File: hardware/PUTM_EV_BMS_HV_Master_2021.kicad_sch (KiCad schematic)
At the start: 22 parts, among them SW1 RESET, U19 STM32F446RETx, Y1 20MHz, Y2 32.768kHz

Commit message: 3d models update, more work on pcb
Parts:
- removed Y2: 32.768kHz, Crystal:Crystal_SMD_3225-4Pin_3.2x2.5mm, symbol Device:Crystal_GND24_Small
- added Y2: 32.768kHz, Crystal:Crystal_SMD_3215-2Pin_3.2x1.5mm, symbol Device:Crystal_Small
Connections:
- net RTC_CLK_IN: now also Y2.2
- net RTC_CLK_OUT: now also Y2.1
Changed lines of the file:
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@@
   (junction (at 252.73 152.4) (diameter 0) (color 0 0 0 0)
-  )
-  (junction (at 245.11 148.59) (diameter 0) (color 0 0 0 0)
   )
   (junction (at 60.96 35.56) (diameter 0) (color 0 0 0 0)
@@
     (stroke (width 0) (type default) (color 0 0 0 0))
   )
-  (wire (pts (xy 245.11 148.59) (xy 245.11 152.4))
-    (stroke (width 0) (type default) (color 0 0 0 0))
-  )
   (wire (pts (xy 117.475 187.325) (xy 118.745 187.325))
     (stroke (width 0) (type default) (color 0 0 0 0))
@@
     (stroke (width 0) (type default) (color 0 0 0 0))
   )
-  (wire (pts (xy 245.11 144.78) (xy 245.11 148.59))
+  (wire (pts (xy 245.11 144.78) (xy 245.11 152.4))
     (stroke (width 0) (type default) (color 0 0 0 0))
   )
@@
     (stroke (width 0) (type default) (color 0 0 0 0))
   )
-  (wire (pts (xy 255.27 148.59) (xy 256.54 148.59))
-    (stroke (width 0) (type default) (color 0 0 0 0))
-  )
   (wire (pts (xy 139.065 147.955) (xy 137.795 147.955))
     (stroke (width 0) (type default) (color 0 0 0 0))
@@
   )
   (wire (pts (xy 38.1 118.11) (xy 40.64 118.11))
-    (stroke (width 0) (type default) (color 0 0 0 0))
-  )
-  (wire (pts (xy 245.11 148.59) (xy 250.19 148.59))
     (stroke (width 0) (type default) (color 0 0 0 0))
   )
@@
     (pin "1")
   )
-  (symbol (lib_id "power:GND") (at 256.54 148.59 90) (unit 1)
-    (in_bom yes) (on_board yes)
-    (property "Reference" "#PWR0166" (id 0) (at 262.89 148.59 0)
-      (effects (font (size 1.27 1.27)) hide)
-    )
-    (property "Value" "GND" (id 1) (at 259.7912 148.463 90)
-      (effects (font (size 1.27 1.27)) (justify right))
-    )
-    (property "Footprint" "" (id 2) (at 256.54 148.59 0)
-      (effects (font (size 1.27 1.27)) hide)
-    )
-    (property "Datasheet" "" (id 3) (at 256.54 148.59 0)
-      (effects (font (size 1.27 1.27)) hide)
-    )
-    (pin "1")
-  )
   (symbol (lib_id "power:GND") (at 224.155 148.59 90) (unit 1)
     (in_bom yes) (on_board yes)
@@
     (pin "4")
   )
-  (symbol (lib_id "Device:Crystal_GND24_Small") (at 252.73 148.59 90) (unit 1)
-    (in_bom yes) (on_board yes)
-    (property "Reference" "Y2" (id 0) (at 255.27 139.7 90))
-    (property "Value" "32.768kHz" (id 1) (at 257.81 141.605 90))
-    (property "Footprint" "Crystal:Crystal_SMD_3225-4Pin_3.2x2.5mm" (id 2) (at 252.73 148.59 0)
+  (symbol (lib_id "Device:Crystal_Small") (at 252.73 148.59 90) (unit 1)
+    (in_bom yes) (on_board yes) (fields_autoplaced)
+    (property "Reference" "Y2" (id 0) (at 255.27 147.3199 90)
+      (effects (font (size 1.27 1.27)) (justify right))
+    )
+    (property "Value" "32.768kHz" (id 1) (at 255.27 149.8599 90)
+      (effects (font (size 1.27 1.27)) (justify right))
+    )
+    (property "Footprint" "Crystal:Crystal_SMD_3215-2Pin_3.2x1.5mm" (id 2) (at 252.73 148.59 0)
       (effects (font (size 1.27 1.27)) hide)
     )
@@
     (pin "1")
     (pin "2")
-    (pin "3")
-    (pin "4")
   )
   (sheet (at 239.395 40.64) (size 26.035 7.62) (fields_autoplaced)
@@
       (reference "#PWR0165") (unit 1) (value "+3.3V") (footprint "")
     )
-    (path "/3bcc80e3-9948-4ec4-868e-16f831c1e740"
-      (reference "#PWR0166") (unit 1) (value "GND") (footprint "")
-    )
     (path "/e61cc821-5479-4c04-b5ab-4a32f17b4f03/3f43c004-d17f-43ac-98bf-c5e9bce1100f"
       (reference "#PWR0167") (unit 1) (value "GND") (footprint "")
@@
       (reference "#PWR0173") (unit 1) (value "GND") (footprint "")
     )
+    (path "/568caa85-d8c4-4885-aabf-c5422dff8b33/5428d4f5-a135-4ff7-981d-717e6e459bc5"
+      (reference "#PWR0174") (unit 1) (value "ISO_GND") (footprint "")
+    )
+    (path "/568caa85-d8c4-4885-aabf-c5422dff8b33/bcd60228-1ed8-4c6e-a1e8-d1f398832a01"
+      (reference "#PWR0175") (unit 1) (value "ISO_GND") (footprint "")
+    )
+    (path "/568caa85-d8c4-4885-aabf-c5422dff8b33/0ac2b524-275c-4685-9499-8b49e50152b4"
+      (reference "#PWR0176") (unit 1) (value "ISO_GND") (footprint "")
+    )
     (path "/6eb4a2b1-8e5b-451b-b593-8aaaa3a4213e/7b3cb172-90a4-4003-9a24-8fe28b6c8d7e"
       (reference "#PWR0184") (unit 1) (value "+5V") (footprint "")
@@
       (reference "#PWR0190") (unit 1) (value "ISO_GND") (footprint "")
     )
-    (path "/568caa85-d8c4-4885-aabf-c5422dff8b33/0ac2b524-275c-4685-9499-8b49e50152b4"
-      (reference "#PWR?") (unit 1) (value "ISO_GND") (footprint "")
-    )
-    (path "/568caa85-d8c4-4885-aabf-c5422dff8b33/5428d4f5-a135-4ff7-981d-717e6e459bc5"
-      (reference "#PWR?") (unit 1) (value "ISO_GND") (footprint "")
-    )
-    (path "/568caa85-d8c4-4885-aabf-c5422dff8b33/bcd60228-1ed8-4c6e-a1e8-d1f398832a01"
-      (reference "#PWR?") (unit 1) (value "ISO_GND") (footprint "")
-    )
     (path "/66c3869d-de11-4d8d-b4de-9d98c32ec205/ddeb9dfe-eb2d-4bf5-bf14-a97849901813"
       (reference "BT1") (unit 1) (value "KEYSTONE 103") (footprint "Battery:BatteryHolder_Keystone_103_1x20mm")
@@
       (reference "L3") (unit 1) (value "33uH") (footprint "Inductor_SMD:L_12x12mm_H8mm")
     )
-    (path "/66c3869d-de11-4d8d-b4de-9d98c32ec205/97f31275-08a9-4ef1-ab6a-111397d3a2f7"
-      (reference "L4") (unit 1) (value "NLV32T-220J-PF") (footprint "Inductor_SMD:L_1210_3225Metric")
-    )
-    (path "/e61cc821-5479-4c04-b5ab-4a32f17b4f03/87282ca0-3147-4352-a9e5-29f84b0fe51e"
-      (reference "L5") (unit 1) (value "NLV32T-220J-PF") (footprint "Inductor_SMD:L_1210_3225Metric")
+    (path "/66c3869d-de11-4d8d-b4de-9d98c32ec205/eb503f36-06f9-429b-bfac-69b2fc2fa2db"
+      (reference "L4") (unit 1) (value "6.8uH") (footprint "Inductor_SMD:L_1206_3216Metric")
+    )
+    (path "/e61cc821-5479-4c04-b5ab-4a32f17b4f03/0422bc5c-79a8-49f4-a2a4-8342195de570"
+      (reference "L5") (unit 1) (value "6.8uH") (footprint "Inductor_SMD:L_1206_3216Metric")
     )
     (path "/81dc0685-0bdd-4dc2-8f76-92836044cf1e/b8954743-0175-4ee0-bad0-8f0716e13306/591c3187-ead2-446d-b183-7d5f2d76f3df"
@@
       (reference "Y1") (unit 1) (value "20MHz") (footprint "Crystal:Crystal_SMD_3225-4Pin_3.2x2.5mm")
     )
-    (path "/b803fbf4-9ceb-446d-ade7-ea57730cfc5e"
-      (reference "Y2") (unit 1) (value "32.768kHz") (footprint "Crystal:Crystal_SMD_3225-4Pin_3.2x2.5mm")
-    )
-  )
+    (path "/ee6556f0-1d2b-4352-82ce-d8d308cb643b"
+      (reference "Y2") (unit 1) (value "32.768kHz") (footprint "Crystal:Crystal_SMD_3215-2Pin_3.2x1.5mm")
+    )
+  )

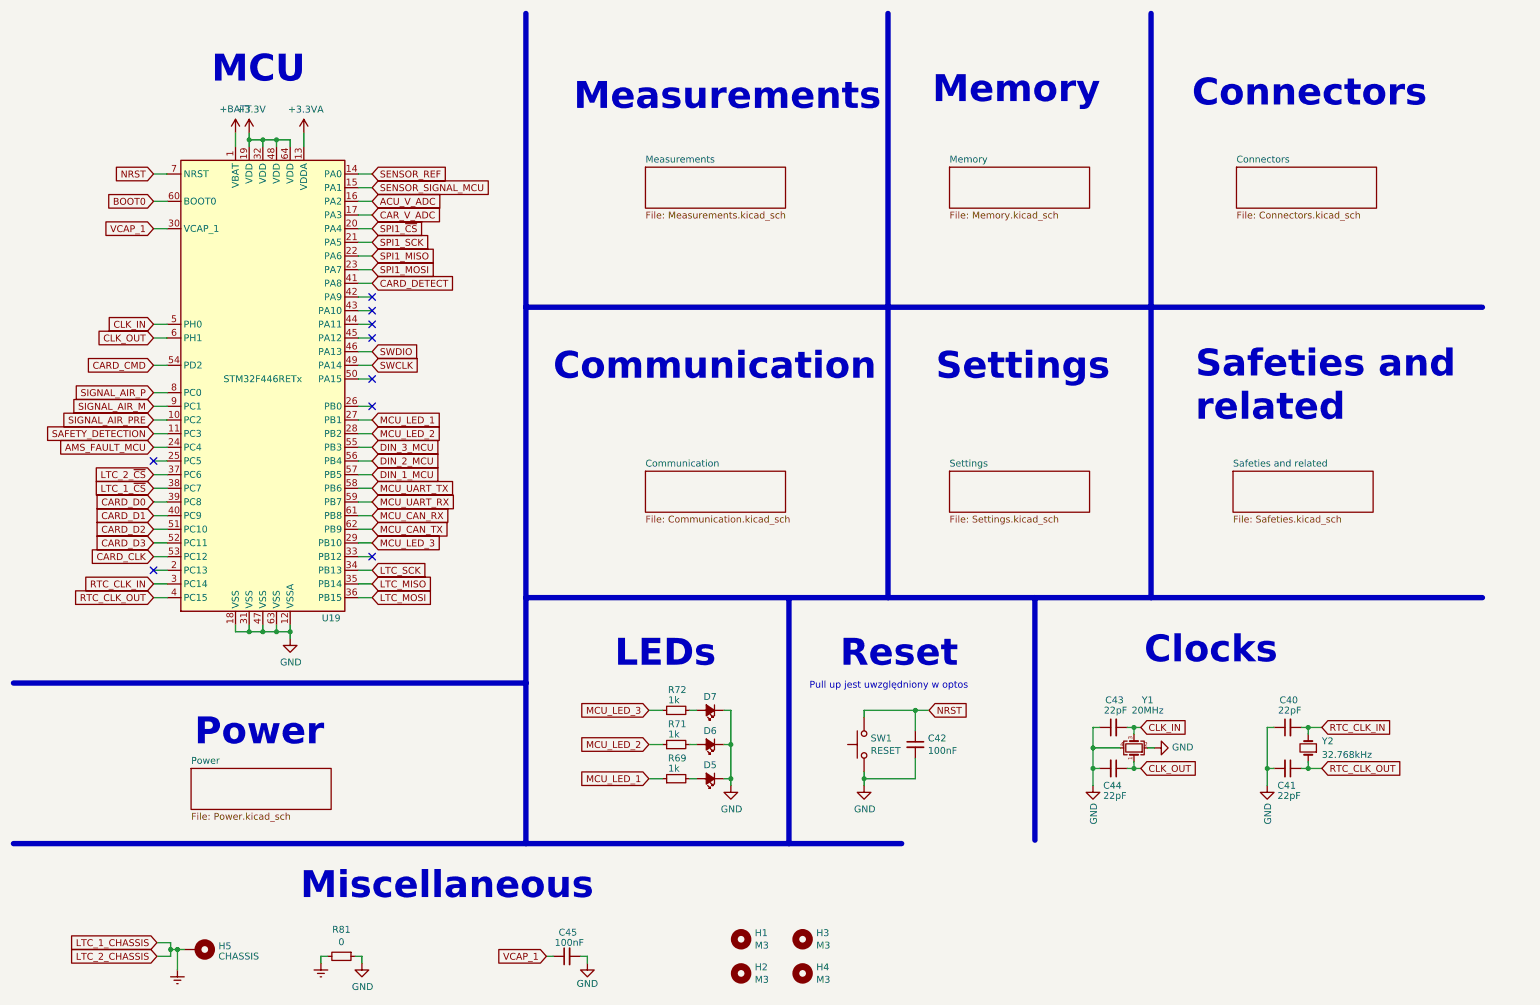
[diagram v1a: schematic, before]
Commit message: Schematic readability update
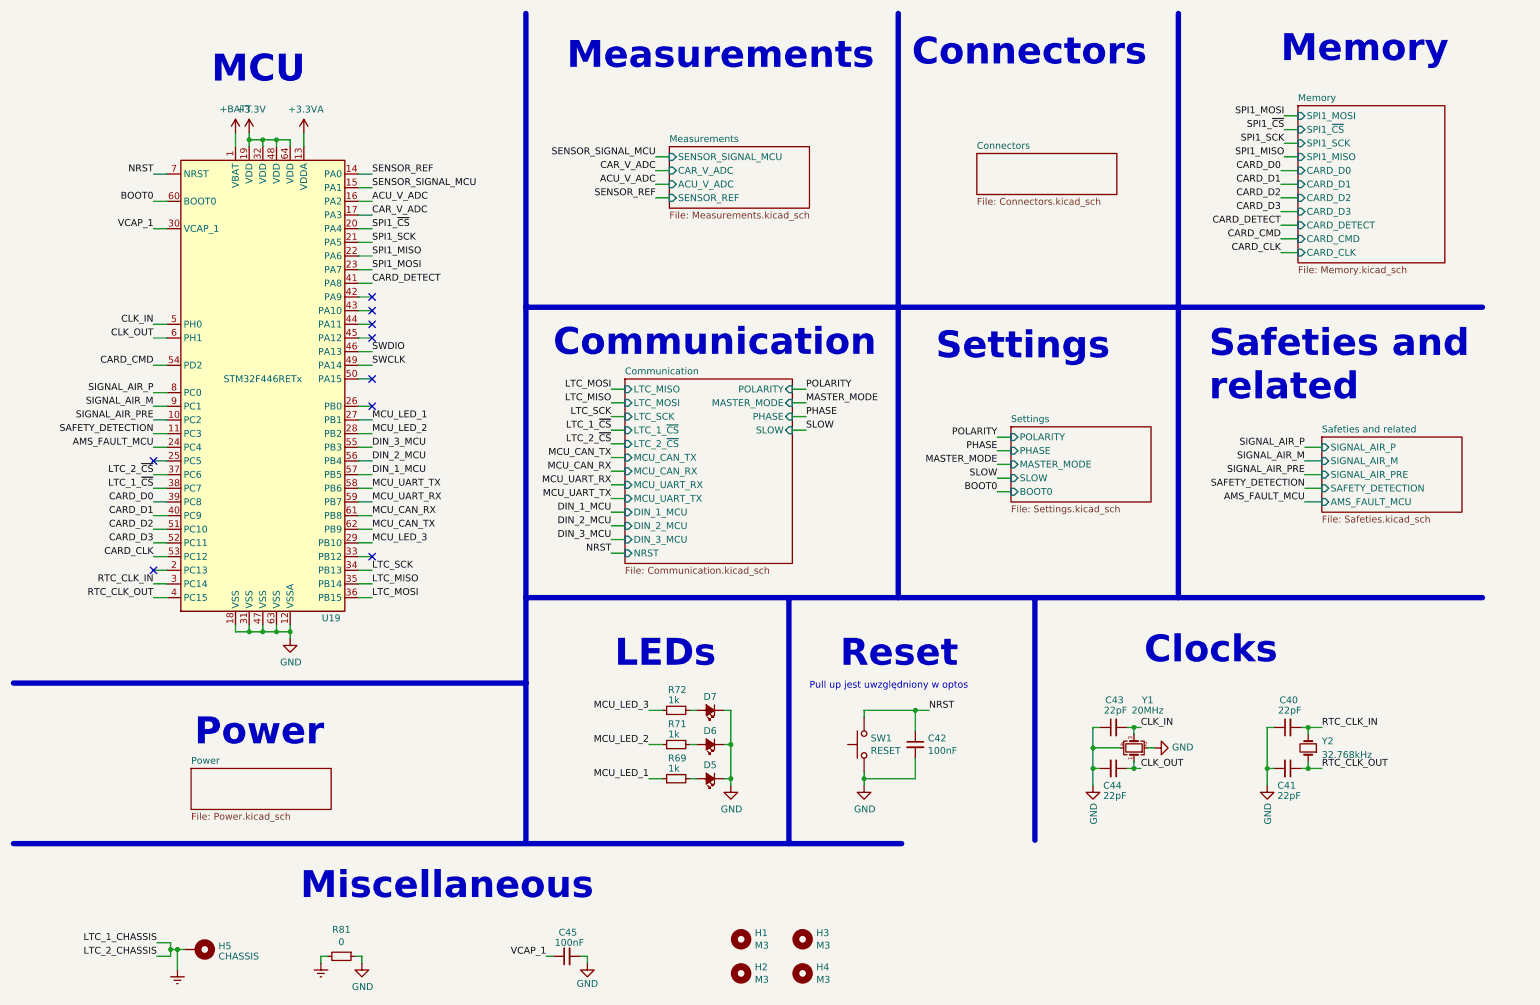
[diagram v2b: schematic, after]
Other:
- sheet Communication ports: added DIN_1_MCU, DIN_2_MCU, DIN_3_MCU, LTC_1_~{CS}, LTC_2_~{CS}, LTC_MISO, LTC_MOSI, LTC_SCK, MASTER_MODE, MCU_CAN_RX, MCU_CAN_TX, MCU_UART_RX, MCU_UART_TX, NRST, PHASE, POLARITY, SLOW; removed none
- sheet Measurements ports: added ACU_V_ADC, CAR_V_ADC, SENSOR_REF, SENSOR_SIGNAL_MCU; removed none
- sheet Memory ports: added CARD_CLK, CARD_CMD, CARD_D0, CARD_D1, CARD_D2, CARD_D3, CARD_DETECT, SPI1_MISO, SPI1_MOSI, SPI1_SCK, SPI1_~{CS}; removed none
- sheet Safeties and related ports: added AMS_FAULT_MCU, SAFETY_DETECTION, SIGNAL_AIR_M, SIGNAL_AIR_P, SIGNAL_AIR_PRE; removed none
- sheet Settings ports: added BOOT0, MASTER_MODE, PHASE, POLARITY, SLOW; removed none

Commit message: finished board design
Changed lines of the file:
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@@
     (effects (font (size 1.27 1.27)) (justify right bottom))
-  )
-  (label "SWDIO" (at 78.74 74.93 0)
-    (effects (font (size 1.27 1.27)) (justify left bottom))
   )
   (label "PHASE" (at 159.385 86.995 0)
@@
     (effects (font (size 1.27 1.27)) (justify right bottom))
   )
-  (label "NRST" (at 38.1 41.91 180)
-    (effects (font (size 1.27 1.27)) (justify right bottom))
-  )
   (label "DIN_1_MCU" (at 123.19 104.775 180)
     (effects (font (size 1.27 1.27)) (justify right bottom))
@@
     (effects (font (size 1.27 1.27)) (justify left bottom))
   )
-  (label "LTC_1_CHASSIS" (at 38.735 184.785 180)
-    (effects (font (size 1.27 1.27)) (justify right bottom))
-  )
   (label "SIGNAL_AIR_M" (at 38.1 85.09 180)
     (effects (font (size 1.27 1.27)) (justify right bottom))
@@
     (effects (font (size 1.27 1.27)) (justify right bottom))
   )
-  (label "LTC_2_CHASSIS" (at 38.735 187.325 180)
-    (effects (font (size 1.27 1.27)) (justify right bottom))
-  )
   (label "MASTER_MODE" (at 159.385 84.455 0)
     (effects (font (size 1.27 1.27)) (justify left bottom))
@@
     (effects (font (size 1.27 1.27)) (justify left bottom))
   )
-  (label "SWCLK" (at 78.74 77.47 0)
-    (effects (font (size 1.27 1.27)) (justify left bottom))
-  )
   (label "SPI1_~{CS}" (at 248.285 33.655 180)
     (effects (font (size 1.27 1.27)) (justify right bottom))
@@
     (effects (font (size 1.27 1.27)) (justify left bottom))
   )
-  (label "NRST" (at 182.245 141.605 0)
-    (effects (font (size 1.27 1.27)) (justify left bottom))
-  )
   (label "CLK_OUT" (at 38.1 72.39 180)
     (effects (font (size 1.27 1.27)) (justify right bottom))
@@
   (label "SIGNAL_AIR_PRE" (at 38.1 87.63 180)
     (effects (font (size 1.27 1.27)) (justify right bottom))
+  )
+  (global_label "LTC_1_CHASSIS" (shape input) (at 38.735 184.785 180) (fields_autoplaced)
+    (effects (font (size 1.27 1.27)) (justify right))
+    (property "Intersheet References" "${INTERSHEET_REFS}" (id 0) (at 22.0779 184.7056 0)
+      (effects (font (size 1.27 1.27)) (justify right) hide)
+    )
+  )
+  (global_label "NRST" (shape input) (at 182.245 141.605 0) (fields_autoplaced)
+    (effects (font (size 1.27 1.27)) (justify left))
+    (property "Intersheet References" "${INTERSHEET_REFS}" (id 0) (at 189.3468 141.5256 0)
+      (effects (font (size 1.27 1.27)) (justify left) hide)
+    )
+  )
+  (global_label "SWDIO" (shape input) (at 78.74 74.93 0) (fields_autoplaced)
+    (effects (font (size 1.27 1.27)) (justify left))
+    (property "Intersheet References" "${INTERSHEET_REFS}" (id 0) (at 86.9304 74.8506 0)
+      (effects (font (size 1.27 1.27)) (justify left) hide)
+    )
+  )
+  (global_label "SWCLK" (shape input) (at 78.74 77.47 0) (fields_autoplaced)
+    (effects (font (size 1.27 1.27)) (justify left))
+    (property "Intersheet References" "${INTERSHEET_REFS}" (id 0) (at 87.2932 77.3906 0)
+      (effects (font (size 1.27 1.27)) (justify left) hide)
+    )
+  )
+  (global_label "NRST" (shape input) (at 38.1 41.91 180) (fields_autoplaced)
+    (effects (font (size 1.27 1.27)) (justify right))
+    (property "Intersheet References" "${INTERSHEET_REFS}" (id 0) (at 30.9982 41.8306 0)
+      (effects (font (size 1.27 1.27)) (justify right) hide)
+    )
+  )
+  (global_label "LTC_2_CHASSIS" (shape input) (at 38.735 187.325 180) (fields_autoplaced)
+    (effects (font (size 1.27 1.27)) (justify right))
+    (property "Intersheet References" "${INTERSHEET_REFS}" (id 0) (at 22.0779 187.2456 0)
+      (effects (font (size 1.27 1.27)) (justify right) hide)
+    )
   )
   (symbol (lib_id "MCU_ST_STM32F4:STM32F446RETx") (at 58.42 80.01 0) (unit 1)
@@
       (reference "#PWR020") (unit 1) (value "+5V") (footprint "")
     )
-    (path "/6eb4a2b1-8e5b-451b-b593-8aaaa3a4213e/082bfc7e-12ba-47b8-86a2-236a96081434"
-      (reference "#PWR024") (unit 1) (value "GND") (footprint "")
-    )
     (path "/66c3869d-de11-4d8d-b4de-9d98c32ec205/6a879ebe-3bb4-4291-9131-53e41ed01927"
       (reference "#PWR025") (unit 1) (value "+5V") (footprint "")
@@
       (reference "#PWR0189") (unit 1) (value "GND") (footprint "")
     )
+    (path "/66c3869d-de11-4d8d-b4de-9d98c32ec205/3f4ed331-990b-4cd9-b359-e3ec57a19f68"
+      (reference "#PWR0190") (unit 1) (value "HV_GND") (footprint "")
+    )
     (path "/66c3869d-de11-4d8d-b4de-9d98c32ec205/2fd65b04-00ca-468e-96ba-af750a3adab4"
-      (reference "#PWR?") (unit 1) (value "HV_+5V") (footprint "")
-    )
-    (path "/66c3869d-de11-4d8d-b4de-9d98c32ec205/3f4ed331-990b-4cd9-b359-e3ec57a19f68"
-      (reference "#PWR?") (unit 1) (value "HV_GND") (footprint "")
+      (reference "#PWR0191") (unit 1) (value "HV_+5V") (footprint "")
     )
     (path "/66c3869d-de11-4d8d-b4de-9d98c32ec205/ddeb9dfe-eb2d-4bf5-bf14-a97849901813"
@@
       (reference "C9") (unit 1) (value "10uF") (footprint "Capacitor_SMD:C_0603_1608Metric")
     )
-    (path "/6eb4a2b1-8e5b-451b-b593-8aaaa3a4213e/24ca4ba1-0bdd-4324-b436-b1dd36ae75a7"
-      (reference "C10") (unit 1) (value "100uF/35V") (footprint "Capacitor_SMD:CP_Elec_8x10")
-    )
     (path "/66c3869d-de11-4d8d-b4de-9d98c32ec205/0f7aa2c6-6387-4f1f-9197-678ff9df4202"
